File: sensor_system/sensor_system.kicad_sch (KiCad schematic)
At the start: 4 parts, among them U4 module_bme280_alt, U5 ESP32-DEVKIT-V1

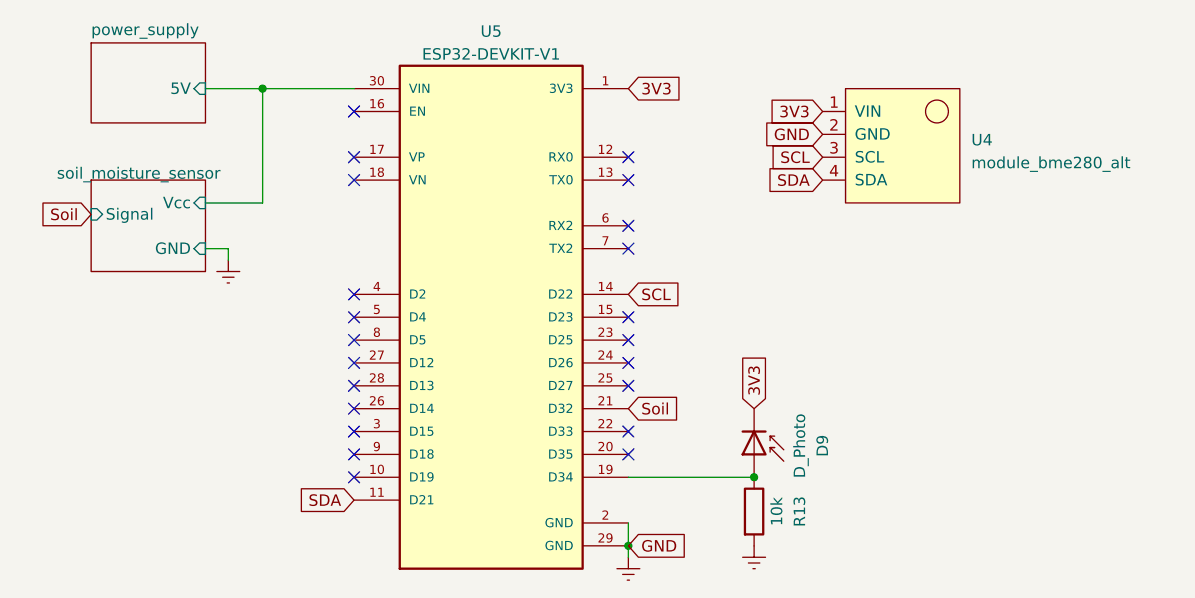
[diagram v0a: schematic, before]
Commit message: Pievienoti footprint visām komponentēm
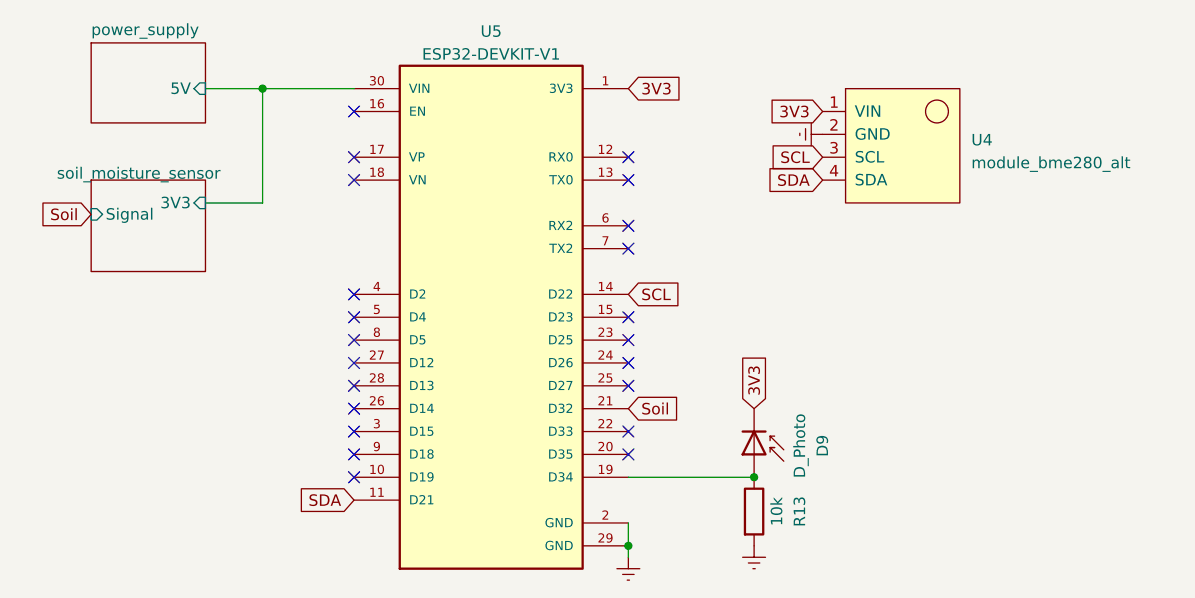
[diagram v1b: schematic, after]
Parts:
- D9: footprint (none) -> LED_THT:LED_D5.0mm
- R13: footprint (none) -> Resistor_SMD:R_0805_2012Metric
- U5: footprint MODULE_ESP32_DEVKIT_V1 -> ESP32-DEVKIT-V1:MODULE_ESP32_DEVKIT_V1
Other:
- sheet soil_moisture_sensor ports: added 3V3; removed GND, Vcc
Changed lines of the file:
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@@
   (no_connect (at 72.39 40.64))
   (no_connect (at 102.87 45.72))
-  (wire (pts (xy 58.42 48.26) (xy 58.42 49.53))
+  (wire (pts (xy 55.88 43.18) (xy 62.23 43.18))
+    (stroke (width 0) (type default))
+  )
+  (wire (pts (xy 55.88 30.48) (xy 62.23 30.48))
+    (stroke (width 0) (type default))
+  )
+  (wire (pts (xy 102.87 73.66) (xy 116.84 73.66))
+    (stroke (width 0) (type default))
+  )
+  (wire (pts (xy 62.23 43.18) (xy 62.23 30.48))
+    (stroke (width 0) (type default))
+  )
+  (wire (pts (xy 102.87 82.55) (xy 102.87 81.28))
     (stroke (width 0) (type default))
   )
@@
     (stroke (width 0) (type default))
   )
-  (wire (pts (xy 55.88 48.26) (xy 58.42 48.26))
-    (stroke (width 0) (type default))
-  )
-  (wire (pts (xy 55.88 43.18) (xy 62.23 43.18))
-    (stroke (width 0) (type default))
-  )
-  (wire (pts (xy 55.88 30.48) (xy 62.23 30.48))
-    (stroke (width 0) (type default))
-  )
-  (wire (pts (xy 102.87 73.66) (xy 116.84 73.66))
-    (stroke (width 0) (type default))
-  )
-  (wire (pts (xy 62.23 43.18) (xy 62.23 30.48))
-    (stroke (width 0) (type default))
-  )
-  (wire (pts (xy 102.87 82.55) (xy 102.87 81.28))
-    (stroke (width 0) (type default))
-  )
   (wire (pts (xy 62.23 30.48) (xy 72.39 30.48))
     (stroke (width 0) (type default))
-  )
-  (global_label "GND" (shape input) (at 124.46 35.56 180) (fields_autoplaced)
-    (effects (font (size 1.27 1.27)) (justify right))
-    (property "Intersheetrefs" "${INTERSHEET_REFS}" (at 117.6837 35.56 0)
-      (effects (font (size 1.27 1.27)) (justify right) hide)
-    )
   )
   (global_label "3V3" (shape input) (at 102.87 30.48 0) (fields_autoplaced)
@@
     )
   )
-  (global_label "GND" (shape input) (at 102.87 81.28 0) (fields_autoplaced)
-    (effects (font (size 1.27 1.27)) (justify left))
-    (property "Intersheetrefs" "${INTERSHEET_REFS}" (at 109.6463 81.28 0)
-      (effects (font (size 1.27 1.27)) (justify left) hide)
-    )
-  )
   (global_label "SDA" (shape input) (at 124.46 40.64 180) (fields_autoplaced)
     (effects (font (size 1.27 1.27)) (justify right))
@@
     )
   )
+  (symbol (lib_id "power:Earth") (at 124.46 35.56 270) (unit 1)
+    (in_bom yes) (on_board yes) (dnp no) (fields_autoplaced)
+    (property "Reference" "#PWR017" (at 118.11 35.56 0)
+      (effects (font (size 1.27 1.27)) hide)
+    )
+    (property "Value" "Earth" (at 120.65 35.56 0)
+      (effects (font (size 1.27 1.27)) hide)
+    )
+    (property "Footprint" "" (at 124.46 35.56 0)
+      (effects (font (size 1.27 1.27)) hide)
+    )
+    (property "Datasheet" "~" (at 124.46 35.56 0)
+      (effects (font (size 1.27 1.27)) hide)
+    )
+    (pin "1")
+    (instances
+      (project "sensor_system"
+        (path "/d745cb62-8f4d-408c-9af8-25e31ee1e0d0"
+          (reference "#PWR017") (unit 1)
+        )
+      )
+    )
+  )
   (symbol (lib_id "Device:D_Photo") (at 116.84 71.12 270) (unit 1)
     (in_bom yes) (on_board yes) (dnp no) (fields_autoplaced)
@@
       (effects (font (size 1.27 1.27)))
     )
-    (property "Footprint" "" (at 116.84 69.85 0)
+    (property "Footprint" "LED_THT:LED_D5.0mm" (at 116.84 69.85 0)
       (effects (font (size 1.27 1.27)) hide)
     )
@@
       (effects (font (size 1.27 1.27)))
     )
-    (property "Footprint" "MODULE_ESP32_DEVKIT_V1" (at 87.63 55.88 0)
+    (property "Footprint" "ESP32-DEVKIT-V1:MODULE_ESP32_DEVKIT_V1" (at 87.63 55.88 0)
       (effects (font (size 1.27 1.27)) (justify bottom) hide)
     )
@@
       (effects (font (size 1.27 1.27)))
     )
-    (property "Footprint" "" (at 115.062 77.47 90)
+    (property "Footprint" "Resistor_SMD:R_0805_2012Metric" (at 115.062 77.47 90)
       (effects (font (size 1.27 1.27)) hide)
     )
@@
         (path "/d745cb62-8f4d-408c-9af8-25e31ee1e0d0"
           (reference "#PWR016") (unit 1)
-        )
-      )
-    )
-  )
-  (symbol (lib_id "power:Earth") (at 58.42 49.53 0) (unit 1)
-    (in_bom yes) (on_board yes) (dnp no) (fields_autoplaced)
-    (property "Reference" "#PWR020" (at 58.42 55.88 0)
-      (effects (font (size 1.27 1.27)) hide)
-    )
-    (property "Value" "Earth" (at 58.42 53.34 0)
-      (effects (font (size 1.27 1.27)) hide)
-    )
-    (property "Footprint" "" (at 58.42 49.53 0)
-      (effects (font (size 1.27 1.27)) hide)
-    )
-    (property "Datasheet" "~" (at 58.42 49.53 0)
-      (effects (font (size 1.27 1.27)) hide)
-    )
-    (pin "1")
-    (instances
-      (project "sensor_system"
-        (path "/d745cb62-8f4d-408c-9af8-25e31ee1e0d0"
-          (reference "#PWR020") (unit 1)
         )
       )
@@
       (effects (font (size 1.27 1.27)) (justify left))
     )
-    (pin "GND" input (at 55.88 48.26 0)
+    (pin "3V3" input (at 55.88 43.18 0)
       (effects (font (size 1.27 1.27)) (justify right))
     )
-    (pin "Vcc" input (at 55.88 43.18 0)
-      (effects (font (size 1.27 1.27)) (justify right))
-    )

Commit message: Disaster in progress
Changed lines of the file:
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@@
   (junction (at 102.87 81.28) (diameter 0) (color 0 0 0 0)
-  )
-  (junction (at 62.23 30.48) (diameter 0) (color 0 0 0 0)
   )
   (no_connect (at 72.39 60.96))
@@
     (stroke (width 0) (type default))
   )
-  (wire (pts (xy 55.88 30.48) (xy 62.23 30.48))
+  (wire (pts (xy 55.88 30.48) (xy 72.39 30.48))
     (stroke (width 0) (type default))
   )
   (wire (pts (xy 102.87 73.66) (xy 116.84 73.66))
-    (stroke (width 0) (type default))
-  )
-  (wire (pts (xy 62.23 43.18) (xy 62.23 30.48))
     (stroke (width 0) (type default))
   )
@@
     (stroke (width 0) (type default))
   )
-  (wire (pts (xy 62.23 30.48) (xy 72.39 30.48))
-    (stroke (width 0) (type default))
-  )
   (global_label "3V3" (shape input) (at 102.87 30.48 0) (fields_autoplaced)
     (effects (font (size 1.27 1.27)) (justify left))
@@
       (effects (font (size 1.27 1.27)) (justify left) hide)
     )
+  )
+  (global_label "3V3" (shape input) (at 62.23 43.18 0) (fields_autoplaced)
+    (effects (font (size 1.27 1.27)) (justify left))
+    (property "Intersheetrefs" "${INTERSHEET_REFS}" (at 68.6434 43.18 0)
+      (effects (font (size 1.27 1.27)) (justify left) hide)
+    )

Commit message: Board V1 with one mistake
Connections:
- net at D9.2 (A), R13.1: now also U5.5 (D4); no longer U5.19 (D34)
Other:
- moved on the sheet: D9, R13
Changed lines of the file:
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@@
 (kicad_sch (version 20230121) (generator eeschema)
   (paper "A4")
-  (junction (at 116.84 73.66) (diameter 0) (color 0 0 0 0)
+  (junction (at 60.96 60.96) (diameter 0) (color 0 0 0 0)
   )
   (junction (at 102.87 81.28) (diameter 0) (color 0 0 0 0)
@@
   (no_connect (at 72.39 73.66))
   (no_connect (at 102.87 58.42))
-  (no_connect (at 72.39 55.88))
+  (no_connect (at 72.39 53.34))
   (no_connect (at 72.39 38.1))
   (no_connect (at 72.39 66.04))
   (no_connect (at 102.87 38.1))
-  (no_connect (at 72.39 53.34))
+  (no_connect (at 102.87 73.66))
   (no_connect (at 72.39 71.12))
   (no_connect (at 72.39 40.64))
   (no_connect (at 102.87 45.72))
+  (wire (pts (xy 63.5 55.88) (xy 72.39 55.88))
+    (stroke (width 0) (type default))
+  )
   (wire (pts (xy 55.88 43.18) (xy 62.23 43.18))
     (stroke (width 0) (type default))
@@
     (stroke (width 0) (type default))
   )
-  (wire (pts (xy 102.87 73.66) (xy 116.84 73.66))
+  (wire (pts (xy 63.5 60.96) (xy 60.96 60.96))
     (stroke (width 0) (type default))
   )
@@
     (stroke (width 0) (type default))
   )
+  (wire (pts (xy 63.5 55.88) (xy 63.5 60.96))
+    (stroke (width 0) (type default))
+  )
   (global_label "3V3" (shape input) (at 102.87 30.48 0) (fields_autoplaced)
     (effects (font (size 1.27 1.27)) (justify left))
@@
     )
   )
-  (global_label "3V3" (shape input) (at 116.84 66.04 90) (fields_autoplaced)
-    (effects (font (size 1.27 1.27)) (justify left))
-    (property "Intersheetrefs" "${INTERSHEET_REFS}" (at 116.84 59.6266 90)
+  (global_label "3V3" (shape input) (at 60.96 53.34 90) (fields_autoplaced)
+    (effects (font (size 1.27 1.27)) (justify left))
+    (property "Intersheetrefs" "${INTERSHEET_REFS}" (at 60.96 46.9266 90)
       (effects (font (size 1.27 1.27)) (justify left) hide)
     )
@@
     )
   )
-  (symbol (lib_id "Device:D_Photo") (at 116.84 71.12 270) (unit 1)
-    (in_bom yes) (on_board yes) (dnp no) (fields_autoplaced)
-    (property "Reference" "D9" (at 124.46 70.1675 0)
-      (effects (font (size 1.27 1.27)))
-    )
-    (property "Value" "D_Photo" (at 121.92 70.1675 0)
-      (effects (font (size 1.27 1.27)))
-    )
-    (property "Footprint" "LED_THT:LED_D5.0mm" (at 116.84 69.85 0)
-      (effects (font (size 1.27 1.27)) hide)
-    )
-    (property "Datasheet" "~" (at 116.84 69.85 0)
+  (symbol (lib_id "Device:D_Photo") (at 60.96 58.42 270) (unit 1)
+    (in_bom yes) (on_board yes) (dnp no) (fields_autoplaced)
+    (property "Reference" "D9" (at 68.58 57.4675 0)
+      (effects (font (size 1.27 1.27)))
+    )
+    (property "Value" "D_Photo" (at 66.04 57.4675 0)
+      (effects (font (size 1.27 1.27)))
+    )
+    (property "Footprint" "LED_THT:LED_D5.0mm" (at 60.96 57.15 0)
+      (effects (font (size 1.27 1.27)) hide)
+    )
+    (property "Datasheet" "~" (at 60.96 57.15 0)
       (effects (font (size 1.27 1.27)) hide)
     )
@@
     )
   )
-  (symbol (lib_id "Device:R") (at 116.84 77.47 0) (unit 1)
-    (in_bom yes) (on_board yes) (dnp no) (fields_autoplaced)
-    (property "Reference" "R13" (at 121.92 77.47 90)
-      (effects (font (size 1.27 1.27)))
-    )
-    (property "Value" "10k" (at 119.38 77.47 90)
-      (effects (font (size 1.27 1.27)))
-    )
-    (property "Footprint" "Resistor_SMD:R_0805_2012Metric" (at 115.062 77.47 90)
-      (effects (font (size 1.27 1.27)) hide)
-    )
-    (property "Datasheet" "~" (at 116.84 77.47 0)
+  (symbol (lib_id "Device:R") (at 60.96 64.77 0) (unit 1)
+    (in_bom yes) (on_board yes) (dnp no) (fields_autoplaced)
+    (property "Reference" "R13" (at 66.04 64.77 90)
+      (effects (font (size 1.27 1.27)))
+    )
+    (property "Value" "10k" (at 63.5 64.77 90)
+      (effects (font (size 1.27 1.27)))
+    )
+    (property "Footprint" "Resistor_SMD:R_0805_2012Metric" (at 59.182 64.77 90)
+      (effects (font (size 1.27 1.27)) hide)
+    )
+    (property "Datasheet" "~" (at 60.96 64.77 0)
       (effects (font (size 1.27 1.27)) hide)
     )
@@
     )
   )
-  (symbol (lib_id "power:Earth") (at 116.84 81.28 0) (unit 1)
-    (in_bom yes) (on_board yes) (dnp no) (fields_autoplaced)
-    (property "Reference" "#PWR016" (at 116.84 87.63 0)
-      (effects (font (size 1.27 1.27)) hide)
-    )
-    (property "Value" "Earth" (at 116.84 85.09 0)
-      (effects (font (size 1.27 1.27)) hide)
-    )
-    (property "Footprint" "" (at 116.84 81.28 0)
-      (effects (font (size 1.27 1.27)) hide)
-    )
-    (property "Datasheet" "~" (at 116.84 81.28 0)
-      (effects (font (size 1.27 1.27)) hide)
-    )
+  (symbol (lib_id "power:Earth") (at 60.96 68.58 0) (unit 1)
+    (in_bom yes) (on_board yes) (dnp no) (fields_autoplaced)
+    (property "Reference" "#PWR016" (at 60.96 74.93 0)
+      (effects (font (size 1.27 1.27)) hide)
+    )
+    (property "Value" "Earth" (at 60.96 72.39 0)
+      (effects (font (size 1.27 1.27)) hide)
+    )
+    (property "Footprint" "" (at 60.96 68.58 0)
+      (effects (font (size 1.27 1.27)) hide)
+    )
+    (property "Datasheet" "~" (at 60.96 68.58 0)
+      (effects (font (size 1.27 1.27)) hide)
+    )

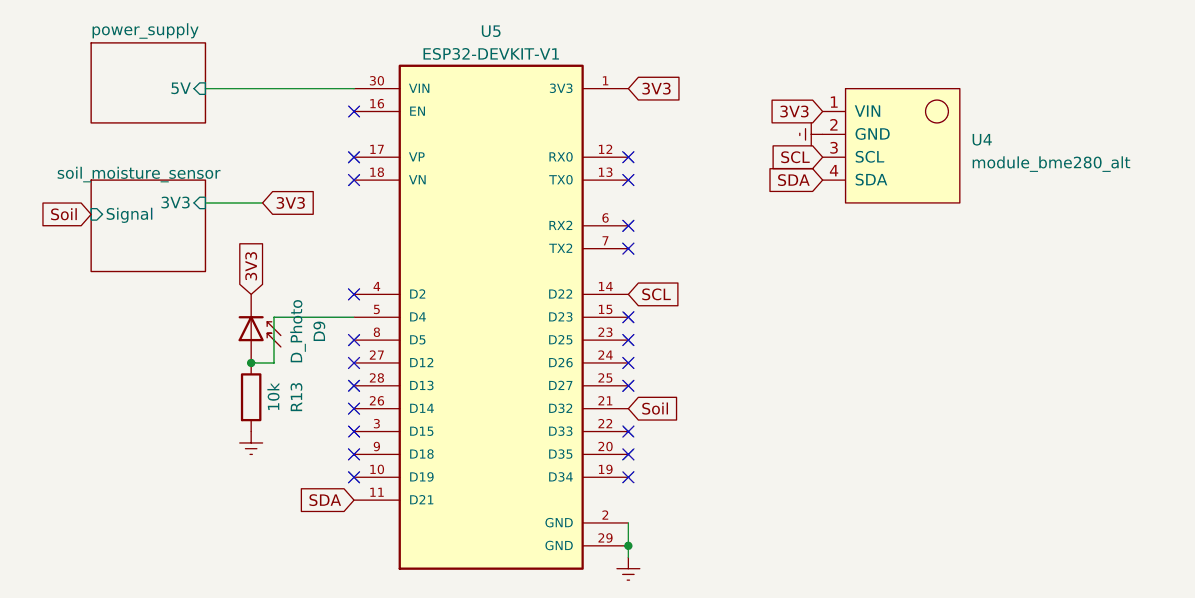
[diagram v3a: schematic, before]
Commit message: BME280 schematic fix
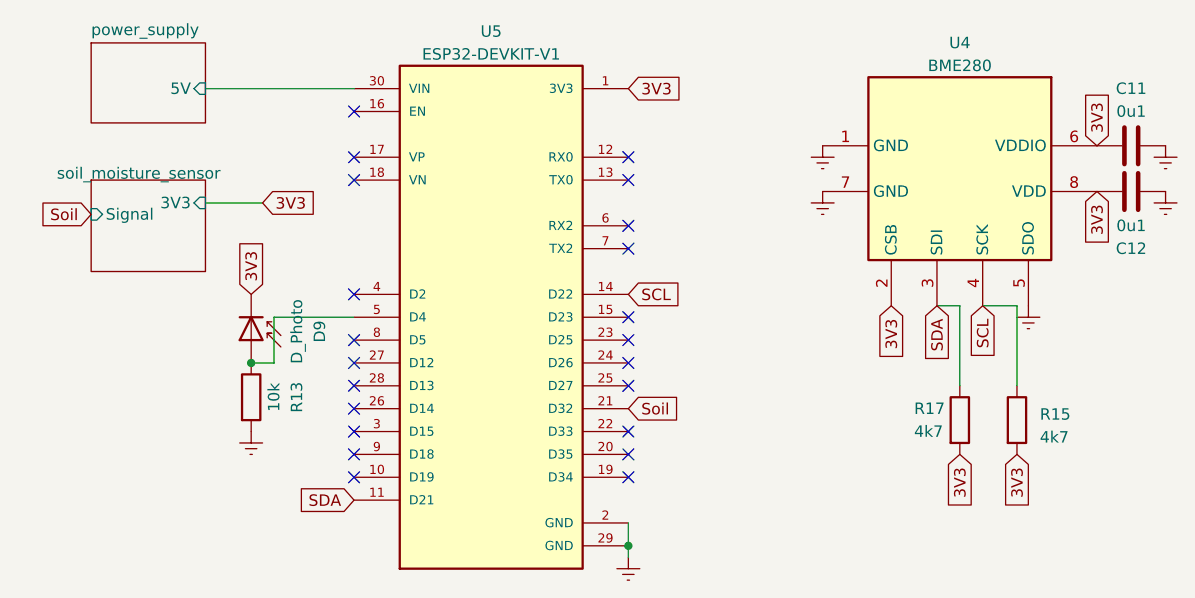
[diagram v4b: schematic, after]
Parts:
- removed U4: module_bme280_alt, usini_sensors:module_bme280_alt, symbol usini_sensors:module_bme280_alt
- added C11, C12: 0u1, symbol Device:C
- added R15, R17: 4k7, symbol Device:R
- added U4: BME280, Package_LGA:Bosch_LGA-8_2.5x2.5mm_P0.65mm_ClockwisePinNumbering, symbol Sensor:BME280
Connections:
- net 3V3: now also C11.1, C12.1, R15.2, R17.2, U4.2 (CSB), U4.6 (VDDIO), U4.8 (VDD)
- net Earth: now also C11.2, C12.2, U4.1 (GND), U4.5 (SDO), U4.7 (GND)
- net SCL: now also R15.1, U4.4 (SCK)
- net SDA: now also R17.1, U4.3 (SDI)
